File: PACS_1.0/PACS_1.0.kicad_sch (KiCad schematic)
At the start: 4 parts, among them U1 MSP430G2553IN20

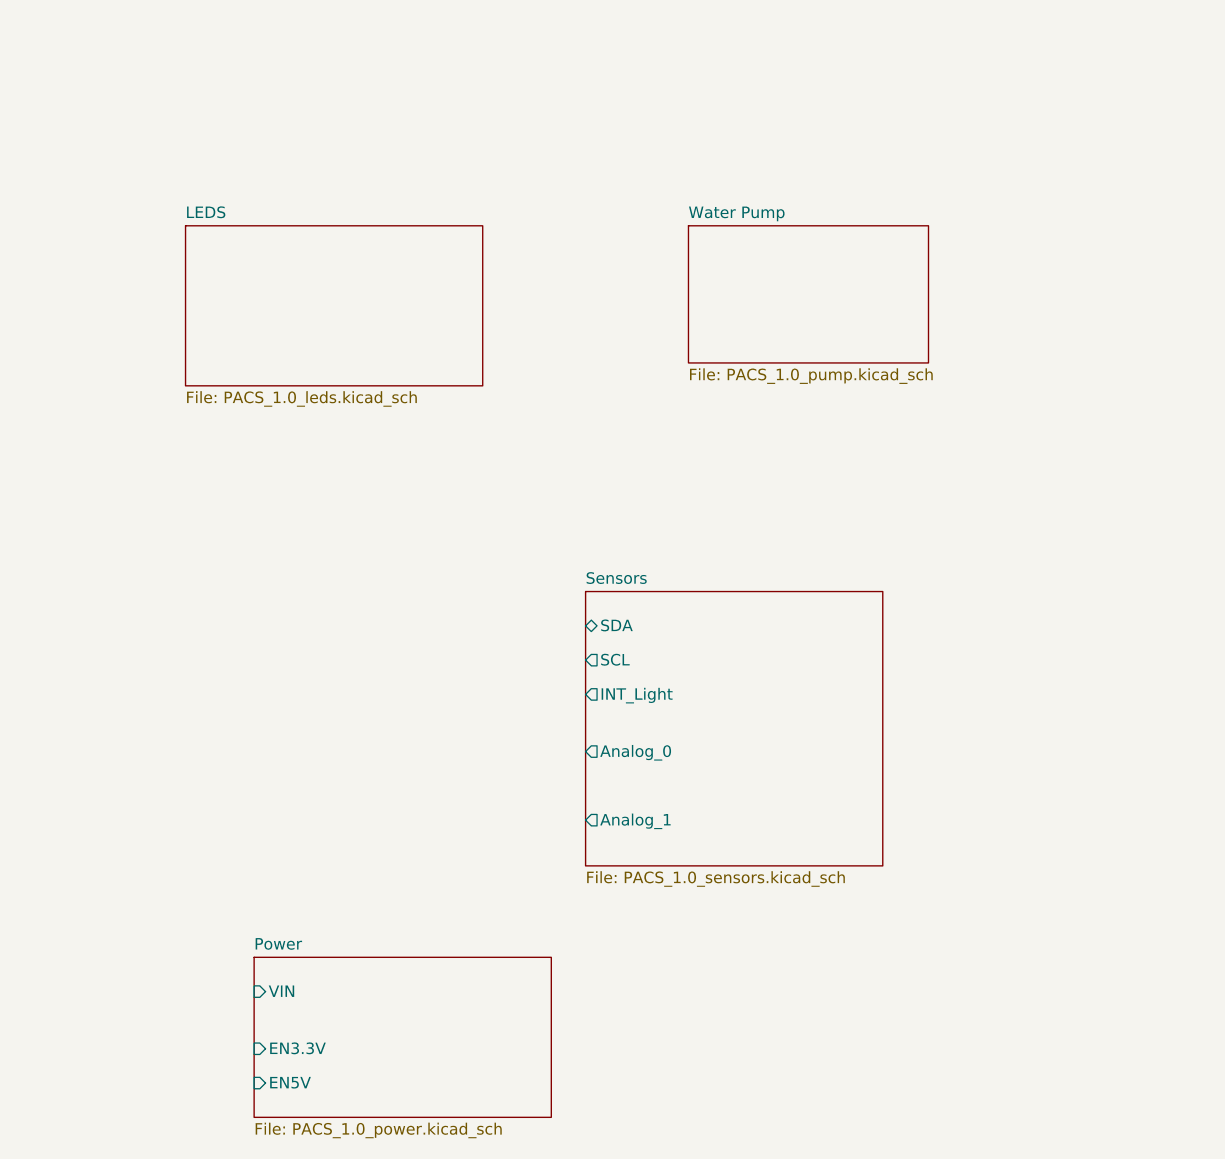
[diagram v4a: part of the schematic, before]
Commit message: Finished water pump, cleaned out empty sheets, added details in 'post its'
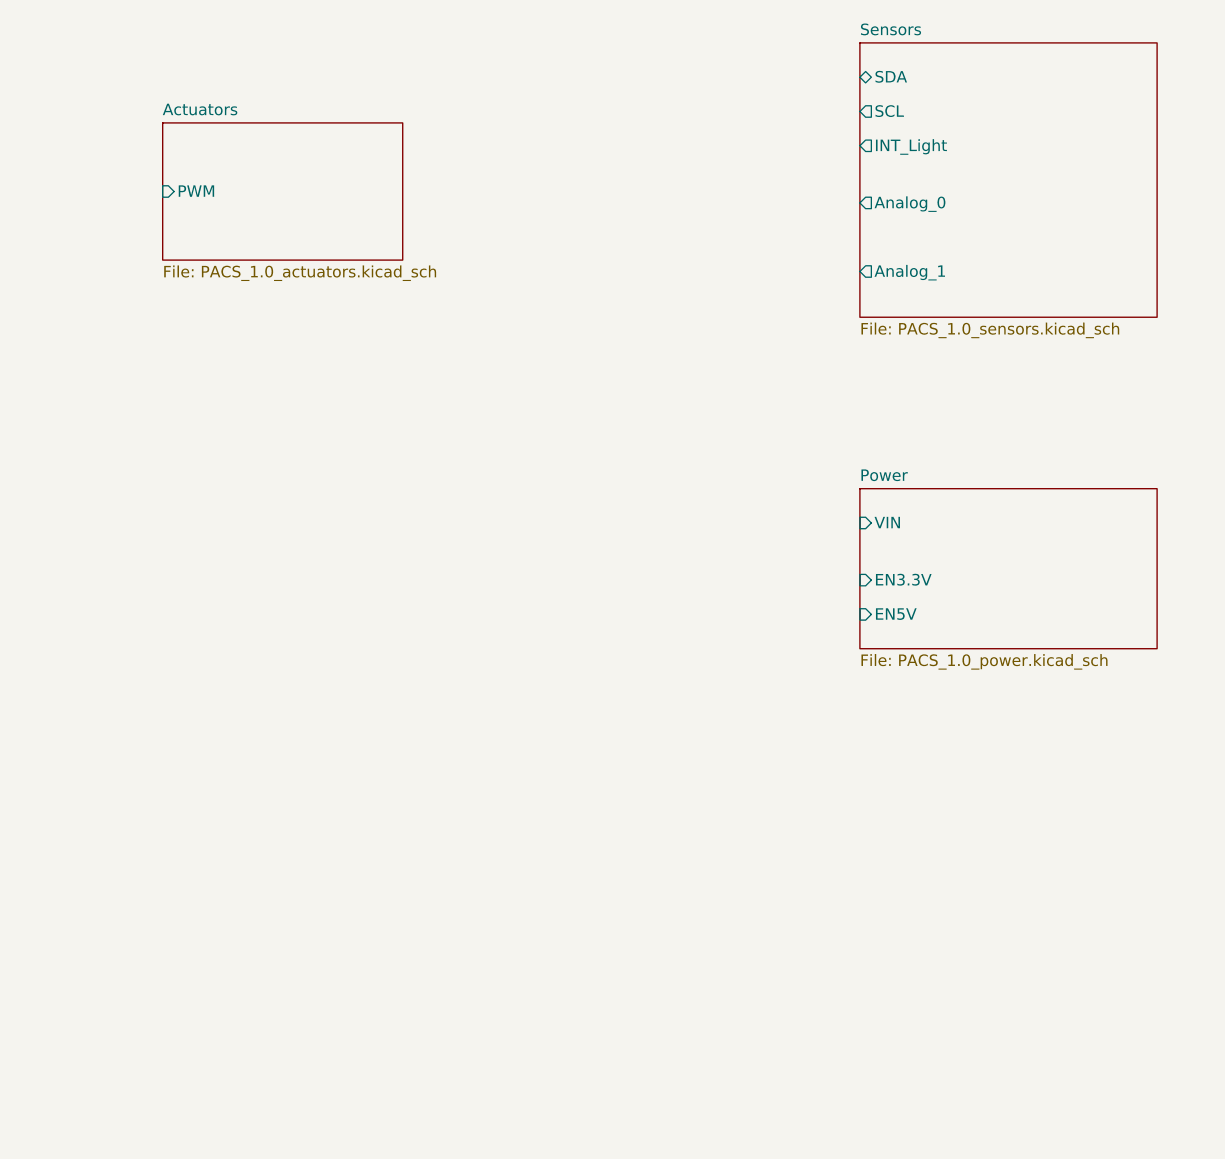
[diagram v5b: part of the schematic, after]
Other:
- sheet Water Pump renamed Actuators
- removed sheet LEDS
- sheet Actuators: file PACS_1.0_pump.kicad_sch -> PACS_1.0_actuators.kicad_sch
- sheet Actuators ports: added PWM; removed none
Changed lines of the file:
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@@
 	)
 	(sheet
-		(at 220.98 38.1)
+		(at 162.56 26.67)
 		(size 26.67 15.24)
 		(fields_autoplaced yes)
@@
 			(color 0 0 0 0.0000)
 		)
-		(property "Sheetname" "Water Pump"
-			(at 220.98 37.3884 0)
+		(property "Sheetname" "Actuators"
+			(at 162.56 25.9584 0)
 			(effects
 				(font
@@
 			)
 		)
-		(property "Sheetfile" "PACS_1.0_pump.kicad_sch"
-			(at 220.98 53.9246 0)
+		(property "Sheetfile" "PACS_1.0_actuators.kicad_sch"
+			(at 162.56 42.4946 0)
 			(effects
 				(font
@@
 			)
 		)
-		(instances
-			(project "PACS_1.0"
-				(path "/6996cbc8-fffb-40fd-8350-2bb7d19e6e7a"
-					(page "5")
-				)
-			)
-		)
-	)
-	(sheet
-		(at 165.1 38.1)
-		(size 33.02 17.78)
-		(fields_autoplaced yes)
-		(stroke
-			(width 0.1524)
-			(type solid)
-		)
-		(fill
-			(color 0 0 0 0.0000)
-		)
-		(property "Sheetname" "LEDS"
-			(at 165.1 37.3884 0)
+		(pin "PWM" input
+			(at 162.56 34.29 180)
 			(effects
 				(font
 					(size 1.27 1.27)
 				)
-				(justify left bottom)
-			)
-		)
-		(property "Sheetfile" "PACS_1.0_leds.kicad_sch"
-			(at 165.1 56.4646 0)
-			(effects
-				(font
-					(size 1.27 1.27)
-				)
-				(justify left top)
+				(justify left)
 			)
 		)
@@
 	)
 	(sheet
-		(at 209.55 78.74)
+		(at 240.03 17.78)
 		(size 33.02 30.48)
 		(fields_autoplaced yes)
@@
 		)
 		(property "Sheetname" "Sensors"
-			(at 209.55 78.0284 0)
+			(at 240.03 17.0684 0)
 			(effects
 				(font
@@
 		)
 		(property "Sheetfile" "PACS_1.0_sensors.kicad_sch"
-			(at 209.55 109.8046 0)
+			(at 240.03 48.8446 0)
 			(effects
 				(font
@@
 		)
 		(pin "SDA" bidirectional
-			(at 209.55 82.55 180)
+			(at 240.03 21.59 180)
 			(effects
 				(font
@@
 		)
 		(pin "SCL" output
-			(at 209.55 86.36 180)
+			(at 240.03 25.4 180)
 			(effects
 				(font
@@
 		)
 		(pin "Analog_0" output
-			(at 209.55 96.52 180)
+			(at 240.03 35.56 180)
 			(effects
 				(font
@@
 		)
 		(pin "INT_Light" output
-			(at 209.55 90.17 180)
+			(at 240.03 29.21 180)
 			(effects
 				(font
@@
 		)
 		(pin "Analog_1" output
-			(at 209.55 104.14 180)
+			(at 240.03 43.18 180)
 			(effects
 				(font
@@
 	)
 	(sheet
-		(at 172.72 119.38)
+		(at 240.03 67.31)
 		(size 33.02 17.78)
 		(fields_autoplaced yes)
@@
 		)
 		(property "Sheetname" "Power"
-			(at 172.72 118.6684 0)
+			(at 240.03 66.5984 0)
 			(effects
 				(font
@@
 		)
 		(property "Sheetfile" "PACS_1.0_power.kicad_sch"
-			(at 172.72 137.7446 0)
+			(at 240.03 85.6746 0)
 			(effects
 				(font
@@
 		)
 		(pin "EN5V" input
-			(at 172.72 133.35 180)
+			(at 240.03 81.28 180)
 			(effects
 				(font
@@
 		)
 		(pin "VIN" input
-			(at 172.72 123.19 180)
+			(at 240.03 71.12 180)
 			(effects
 				(font
@@
 		)
 		(pin "EN3.3V" input
-			(at 172.72 129.54 180)
+			(at 240.03 77.47 180)
 			(effects
 				(font

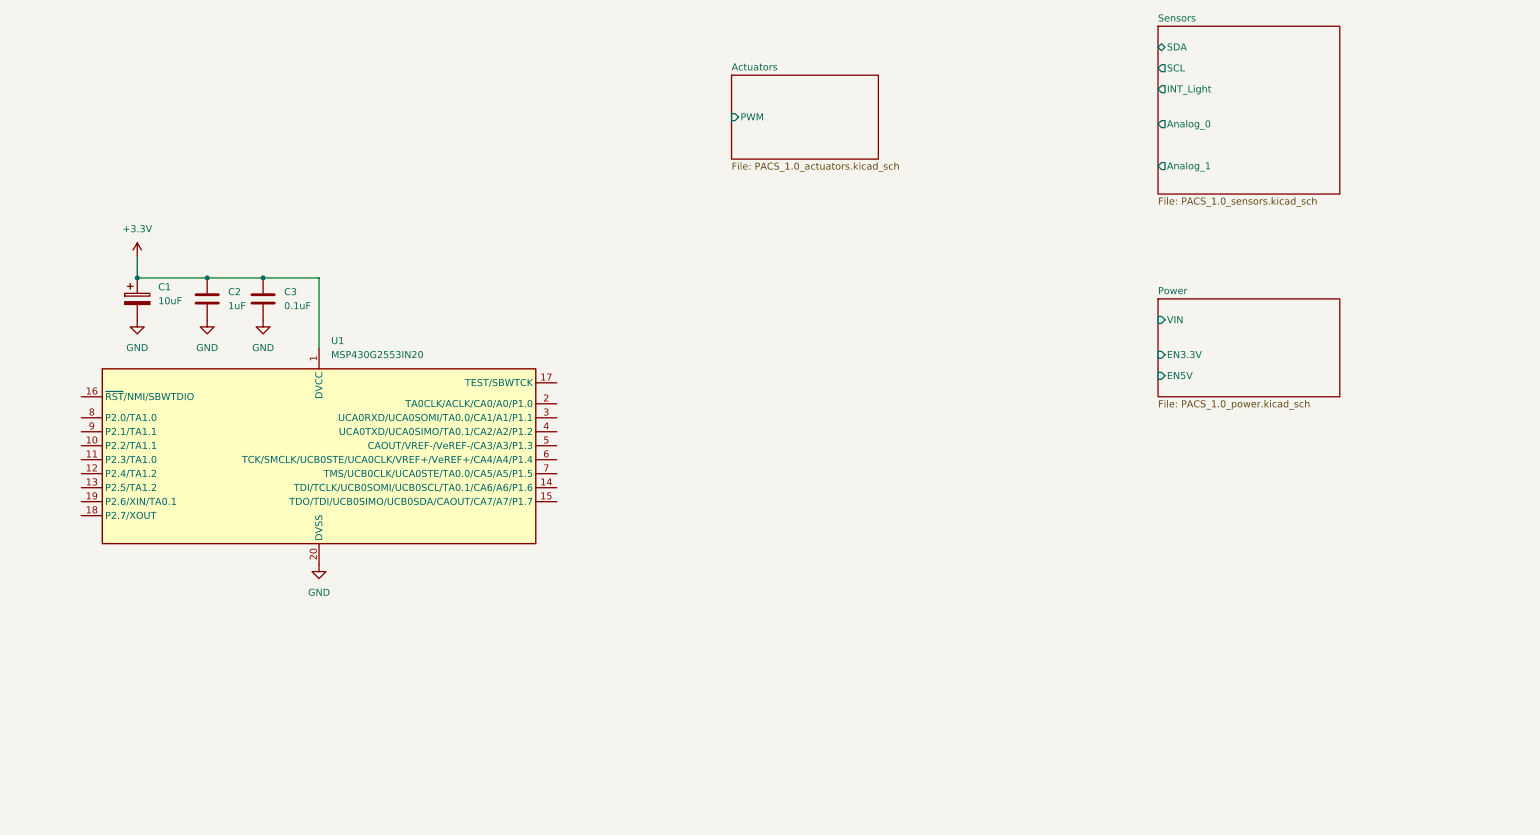
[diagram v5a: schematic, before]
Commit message: Finished Zigbee Module
also fixed some library issues
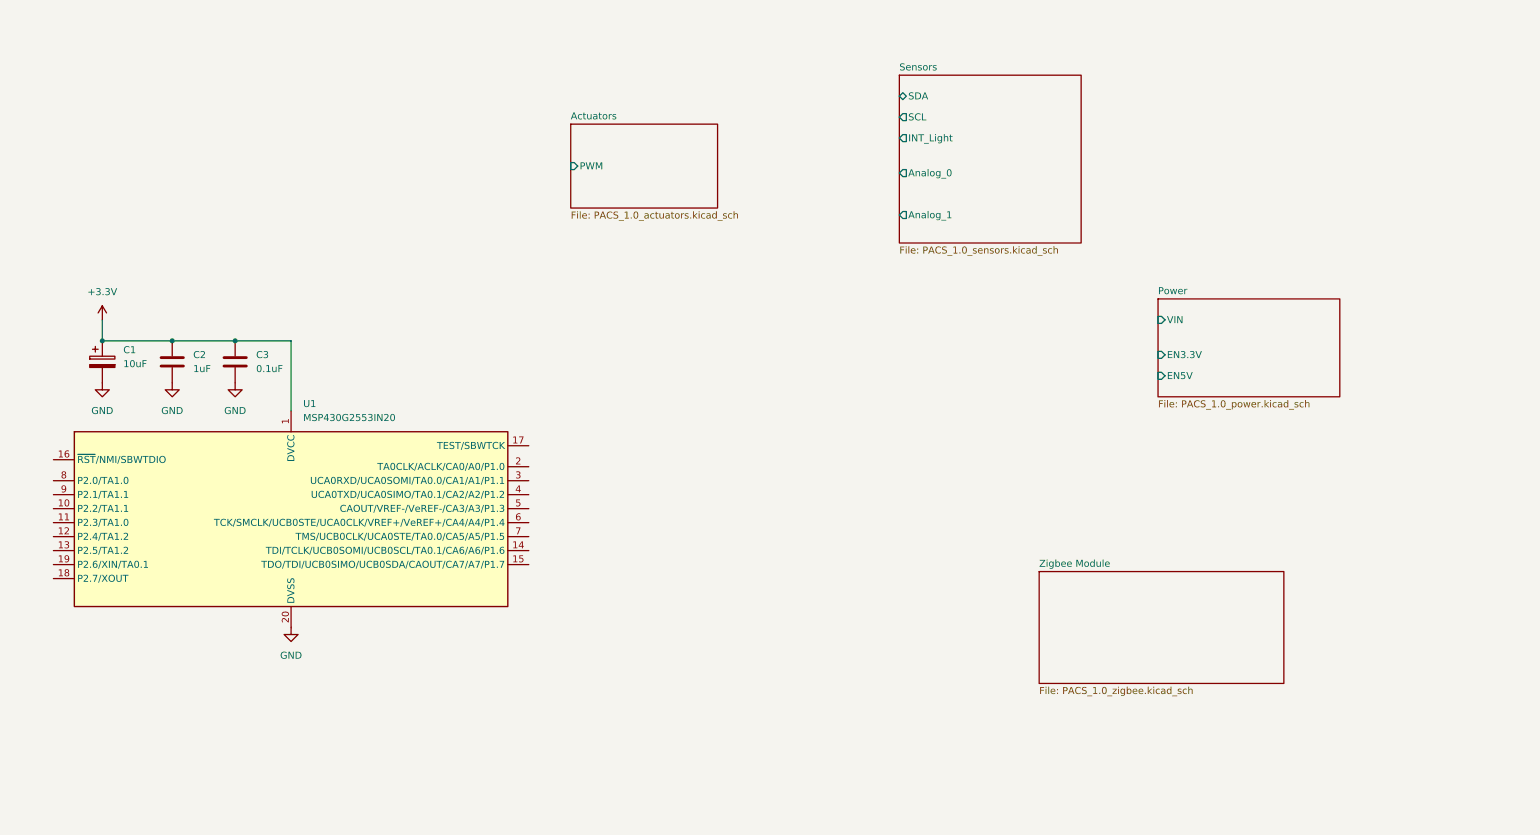
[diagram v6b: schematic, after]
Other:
- added sheet Zigbee Module (PACS_1.0_zigbee.kicad_sch)
- moved on the sheet: C1, C2, C3, U1

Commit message: Finished 1.0 (NO INA INCLUDED)
Finished PACS 1.0 sheets, Power sheet needs considerations, no INA yet.
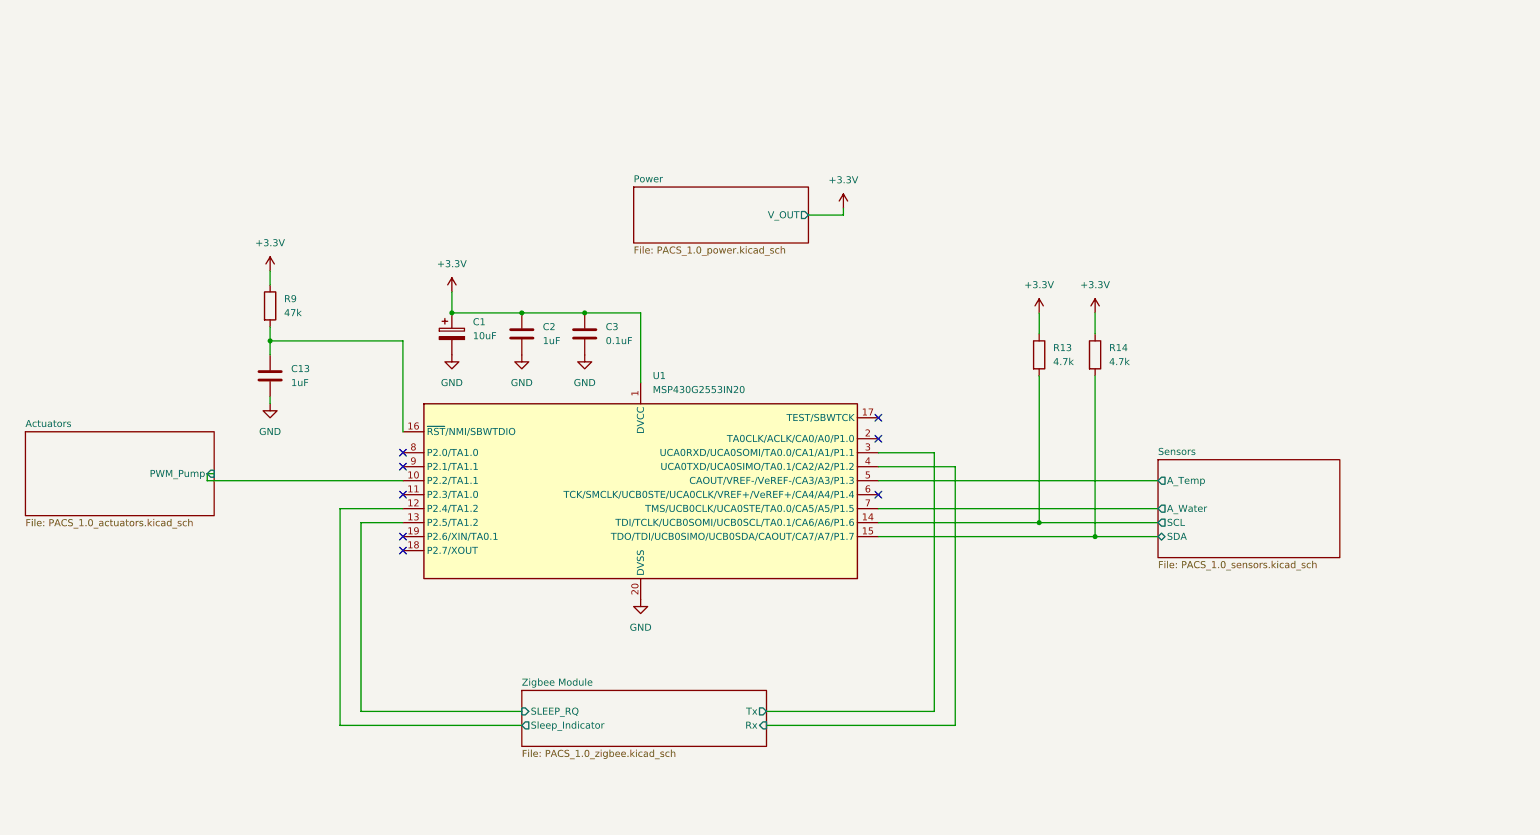
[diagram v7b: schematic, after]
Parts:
- added C13: 1uF, symbol Device:C
- added R13, R14: 4.7k, symbol Device:R
- added R9: 47k, symbol Device:R
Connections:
- net +3.3V: now also R13.1, R14.1, R9.1
- net GND: now also C13.2
- net Sensors/SCL: now also U1.14 (TDI/TCLK/UCB0SOMI/UCB0SCL/TA0.1/CA6/A6/P1.6), R13.2
- net Sensors/SDA: now also U1.15 (TDO/TDI/UCB0SIMO/UCB0SDA/CAOUT/CA7/A7/P1.7), R14.2
- net Actuators/PWM_Pump: now reaches U1.10 (P2.2/TA1.1)
- net Zigbee Module/Sleep_Indicator: now reaches U1.12 (P2.4/TA1.2)
- net Zigbee Module/SLEEP_RQ: now reaches U1.13 (P2.5/TA1.2)
- net at U1.16 (~{RST}/NMI/SBWTDIO): now also C13.1, R9.2
- net Zigbee Module/Tx: now reaches U1.3 (UCA0RXD/UCA0SOMI/TA0.0/CA1/A1/P1.1)
- net Zigbee Module/Rx: now reaches U1.4 (UCA0TXD/UCA0SIMO/TA0.1/CA2/A2/P1.2)
- net Sensors/A_Temp: now reaches U1.5 (CAOUT/VREF-/VeREF-/CA3/A3/P1.3)
- net Sensors/A_Water: now reaches U1.7 (TMS/UCB0CLK/UCA0STE/TA0.0/CA5/A5/P1.5)
- no-connect marks 0 -> 8
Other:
- sheet Actuators ports: added PWM_Pump; removed PWM
- sheet Power ports: added V_OUT; removed EN3.3V, EN5V, VIN
- sheet Sensors ports: added A_Temp, A_Water; removed Analog_0, Analog_1, INT_Light
- sheet Zigbee Module ports: added Rx, SLEEP_RQ, Sleep_Indicator, Tx; removed none
- title: Main Sheet -> MCU and Connections
- moved on the sheet: C1, C2, C3, U1

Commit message: COMPLETE PACS v1.0
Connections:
- net Power/A_Voltage: now reaches U1.6 (TCK/SMCLK/UCB0STE/UCA0CLK/VREF+/VeREF+/CA4/A4/P1.4)
- net Power/VD_ON/OFF: now reaches U1.8 (P2.0/TA1.0)
- no-connect marks 8 -> 6
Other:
- sheet Power ports: added A_Voltage, VD_ON/OFF; removed none
- moved on the sheet: C13, R9
